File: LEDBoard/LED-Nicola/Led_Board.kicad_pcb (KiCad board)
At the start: 2 copper layers, 107.9 x 67.3 mm, 37 parts, among them J1 MOUNTING_HOLE, J10 CONN_01X02, J101 CONN_01X05, J11 LED CONN 01X16, J12 CONN_01X02, J13 LED CONN 01X04, J2 MOUNTING_HOLE, J3 MOUNTING_HOLE, J4 MOUNTING_HOLE, J6 Arduino CONN_01X04, J7 Arduino CONN_01X06, J8 VD 0 CONN_01X02, J9 CONN_01X02, Q1 MMBT, U1 SSR

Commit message: Final changes
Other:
- board text added: "Nicola Duffy Paradigm 2017 LED Board"
- board text removed: "Nicola Duffy Paradigm 2017"
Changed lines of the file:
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@@
       (xy 0.004605 -5.919414) (xy 0.072011 -5.919134)) (layer F.SilkS) (width 0.01))
   )
-  (gr_text "Nicola Duffy\nParadigm 2017" (at 86.36 99.06 90) (layer F.SilkS)
-    (effects (font (size 0.7 0.7) (thickness 0.1)))
+  (gr_text "Nicola Duffy\nParadigm 2017\nLED Board\n" (at 121.666 78.867) (layer F.SilkS)
+    (effects (font (size 1 1) (thickness 0.2)))
   )
   (gr_text "Arduino Inputs\nOrder: LED 1, Buzzer 1, LED 2-9, 24V, 5V, Buzzer 2, GND" (at 125.73 96.52) (layer F.SilkS)

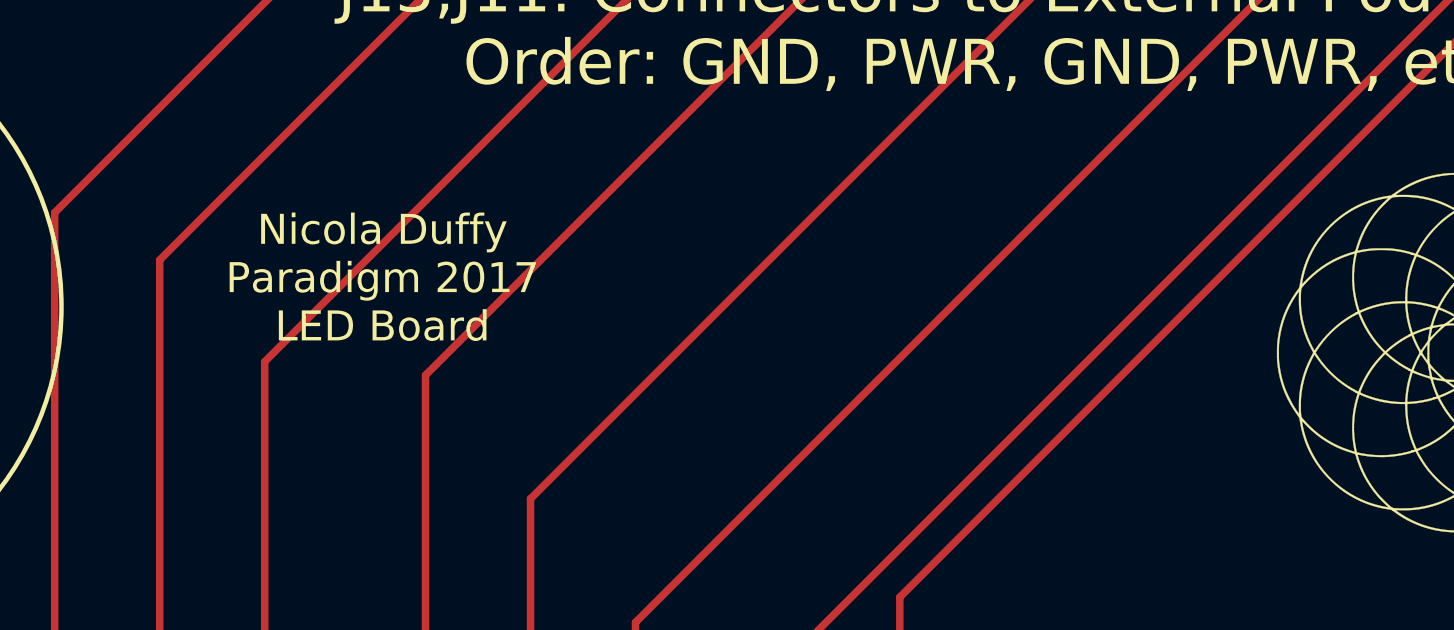
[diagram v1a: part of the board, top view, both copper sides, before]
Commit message: small silkscreen change - copyright and version location
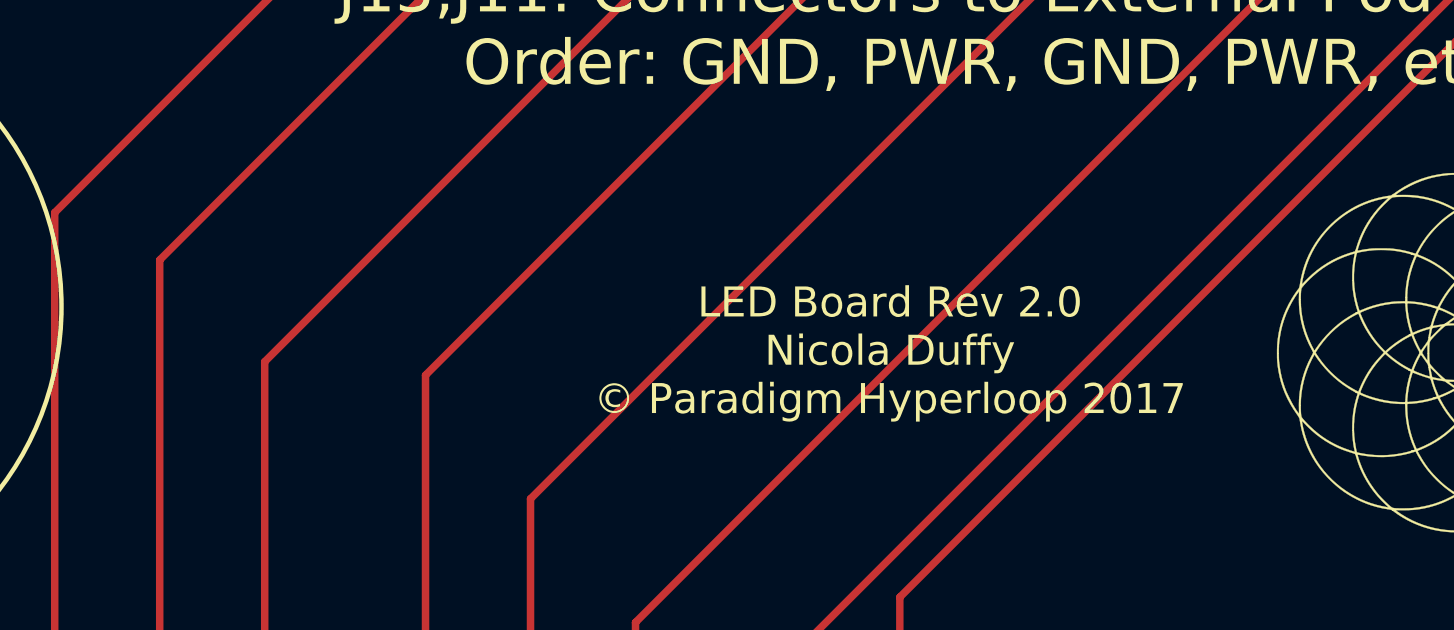
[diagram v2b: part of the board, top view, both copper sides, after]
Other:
- board text added: "LED Board Rev 2.0 Nicola Duffy © Paradigm Hyperloop 2017"
- board text removed: "Nicola Duffy Paradigm 2017 LED Board"
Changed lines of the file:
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@@
-(kicad_pcb (version 4) (host pcbnew 4.0.6)
+(kicad_pcb (version 4) (host pcbnew 4.0.4-stable)
   (general
     (links 61)
@@
       (xy 0.004605 -5.919414) (xy 0.072011 -5.919134)) (layer F.SilkS) (width 0.01))
   )
-  (gr_text "Nicola Duffy\nParadigm 2017\nLED Board\n" (at 121.666 78.867) (layer F.SilkS)
+  (gr_text "LED Board Rev 2.0\nNicola Duffy\n© Paradigm Hyperloop 2017\n\n" (at 138.5824 82.0928) (layer F.SilkS)
     (effects (font (size 1 1) (thickness 0.2)))
   )
